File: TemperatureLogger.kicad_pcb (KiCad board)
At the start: 2 copper layers, 33 x 53 mm, 12 parts, among them J1 USB_A, SW1 RESET, SW2 A, SW3 B, SW4 MODE, U1 DHT11, U2 UA78M33_TO252, U3 ESP-12E, U4 TTL

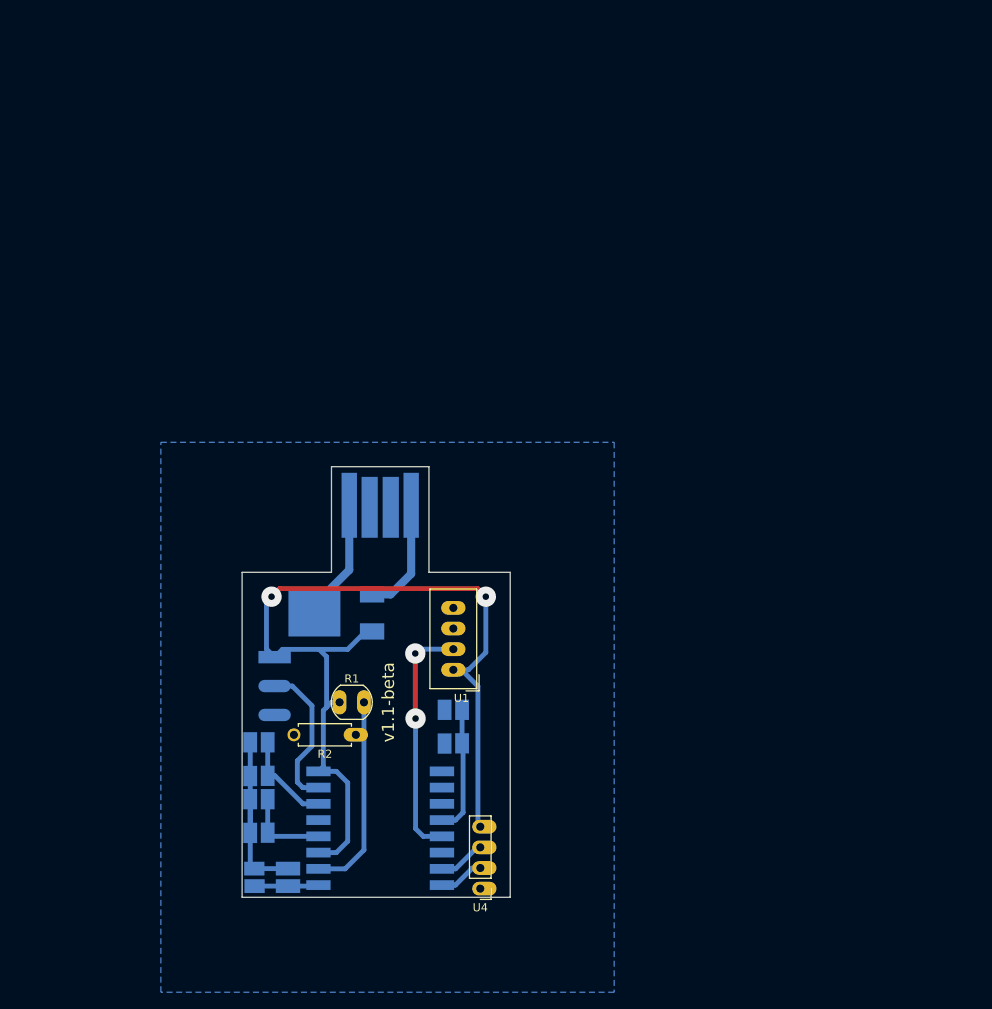
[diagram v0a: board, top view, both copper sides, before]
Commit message: Add main components
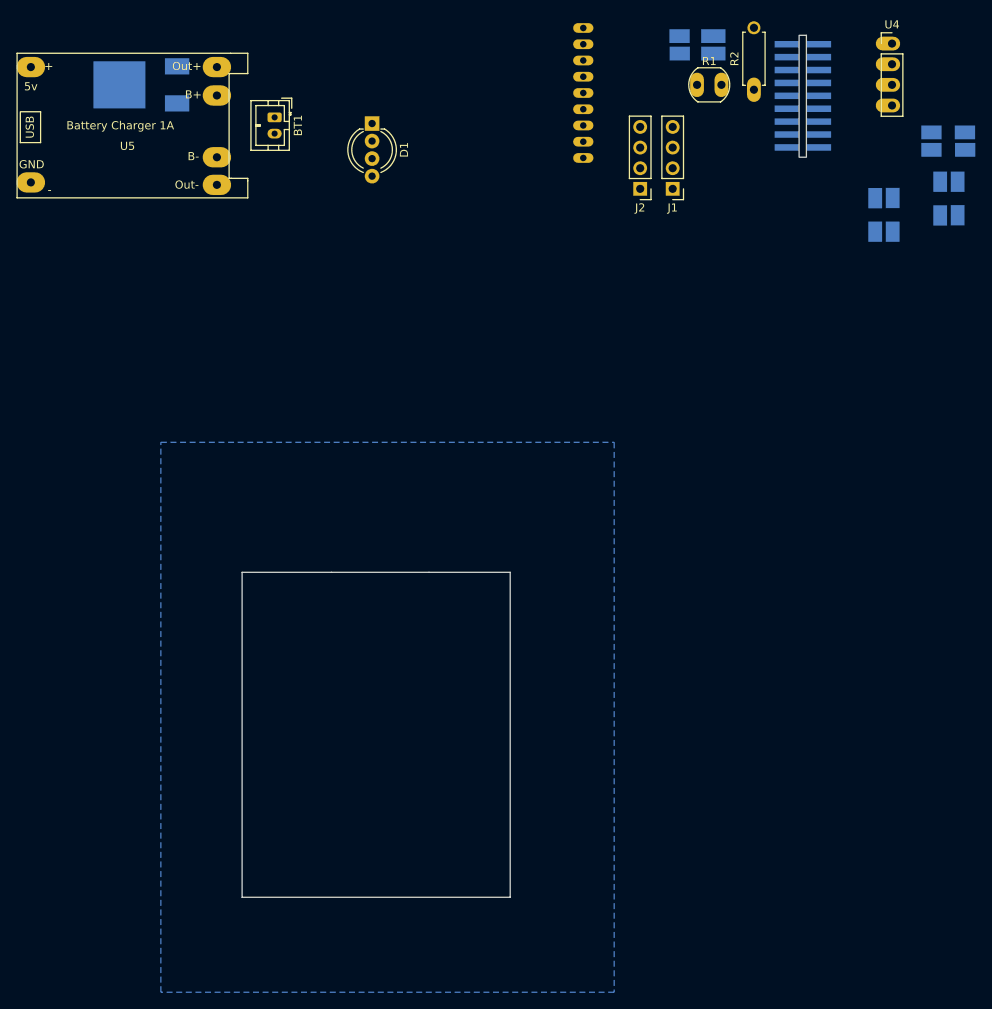
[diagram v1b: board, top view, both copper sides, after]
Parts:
- removed LIN1: LEDs_In, neopixel-strip:neopixel-strip
- removed U1: DHT11, Sensor:Aosong_DHT11_5.5x12.0_P2.54mm
- added BT1: Battery_Cell, Connector_JST:JST_PH_B2B-PH-K_1x02_P2.00mm_Vertical, F.Cu at (87.0, 25.0)
- added D1: WS2812B, LED_THT:LED_D5.0mm-4_RGB_Wide_Pins, F.Cu at (99.0, 25.8)
- added J2: I2C, Connector_PinHeader_2.54mm:PinHeader_1x04_P2.54mm_Vertical, F.Cu at (132.0, 33.8)
- added J3: Micro_SD_Card, sd-card:sd-card, B.Cu at (125.0, 22.0)
- added U5: tp4056, tp4056:tp4056, F.Cu at (68.0, 26.0)
- J1: value USB_A -> I2C; footprint usb-a-pcb:usb-a-pcb -> Connector_PinHeader_2.54mm:PinHeader_1x04_P2.54mm_Vertical; moved to F.Cu
- U3: value ESP-12E -> esp-01m; footprint RF_Module:ESP-12E -> esp-01m:esp-01m
- moved SW2 118.7 mm to (169.9, 27.9), turned to 0 degrees
- moved U4 115.7 mm to (163.0, 15.9), turned to 0 degrees
- moved SW1 115.1 mm to (138.9, 16.1)
- moved SW3 109.4 mm to (170.0, 35.0)
- moved U3 107.1 mm to (152.0, 22.4), turned to 180 degrees
- moved R2 93.3 mm to (146.0, 21.6), turned to 90 degrees
- moved R1 87.8 mm to (139.0, 21.0)
- moved SW4 82.3 mm to (162.0, 37.0), turned to 90 degrees
- moved U2 69.3 mm to (70.0, 21.0)
- moved J1 49.6 mm to (136.0, 33.8)
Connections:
- J1 pad 1: +5V -> +3V3
- J1 pad 2: unconnected-(J1-Pad2) -> GND
- J1 pad 3: unconnected-(J1-Pad3) -> I2C_CLK
- J1 pad 4: GND -> I2C_SDA
- R1 pad 2: Net-(U3-Pad2) -> Net-(R1-Pad2)
- R2 pad 1: Net-(U3-Pad2) -> Net-(R1-Pad2)
- U3 pad 1: Net-(SW1-Pad2) -> GND
- U3 pad 15: GND -> SPI_SS
- U3 pad 16: GND -> Net-(R1-Pad2)
- U3 pad 17: unconnected-(U3-Pad17) -> Net-(SW1-Pad2)
- U3 pad 18: Net-(SW4-Pad2) -> Net-(SW1-Pad2)
- U3 pad 2: Net-(U3-Pad2) -> +3V3
- U3 pad 3: +3V3 -> TX
- U3 pad 4: BUTTON-A -> RX
- U3 pad 5: unconnected-(U3-Pad5) -> NEOPIXEL
- U3 pad 6: BUTTON-B -> BUTTON-A
- U3 pad 7: NEOPIXEL -> BUTTON-B
- U3 pad 8: +3V3 -> Net-(SW4-Pad2)
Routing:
- net +3V3: track 114.1 -> 0.00 mm, vias 2 -> 0
- net GND: track 39.1 -> 0.00 mm
- net TEMP: track 30.1 -> 0.00 mm, vias 2 -> 0
- net Net-(U3-Pad2): track 25.7 -> 0.00 mm
- net NEOPIXEL: track 18.6 -> 0.00 mm
- net +5V: track 15.1 -> 0.00 mm
- net Net-(SW4-Pad2): track 14.9 -> 0.00 mm
- net BUTTON-B: track 11.8 -> 0.00 mm
- net BUTTON-A: track 10.6 -> 0.00 mm
- net Net-(SW1-Pad2): track 7.92 -> 0.00 mm
- net RX: track 5.81 -> 0.00 mm
- net TX: track 5.59 -> 0.00 mm
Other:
- board size 33 x 53 mm -> 33 x 40 mm
- board text removed: "COVER!"
- board text removed: "TODO: - Neopixel needs more space and flat underground - Switches pads need to move to the outside of the switch - Fix DHT11 - Neopixel add header 3 x connector"
- board text removed: "v1.1-beta"

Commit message: Add bme280 sensor and as12ap switch
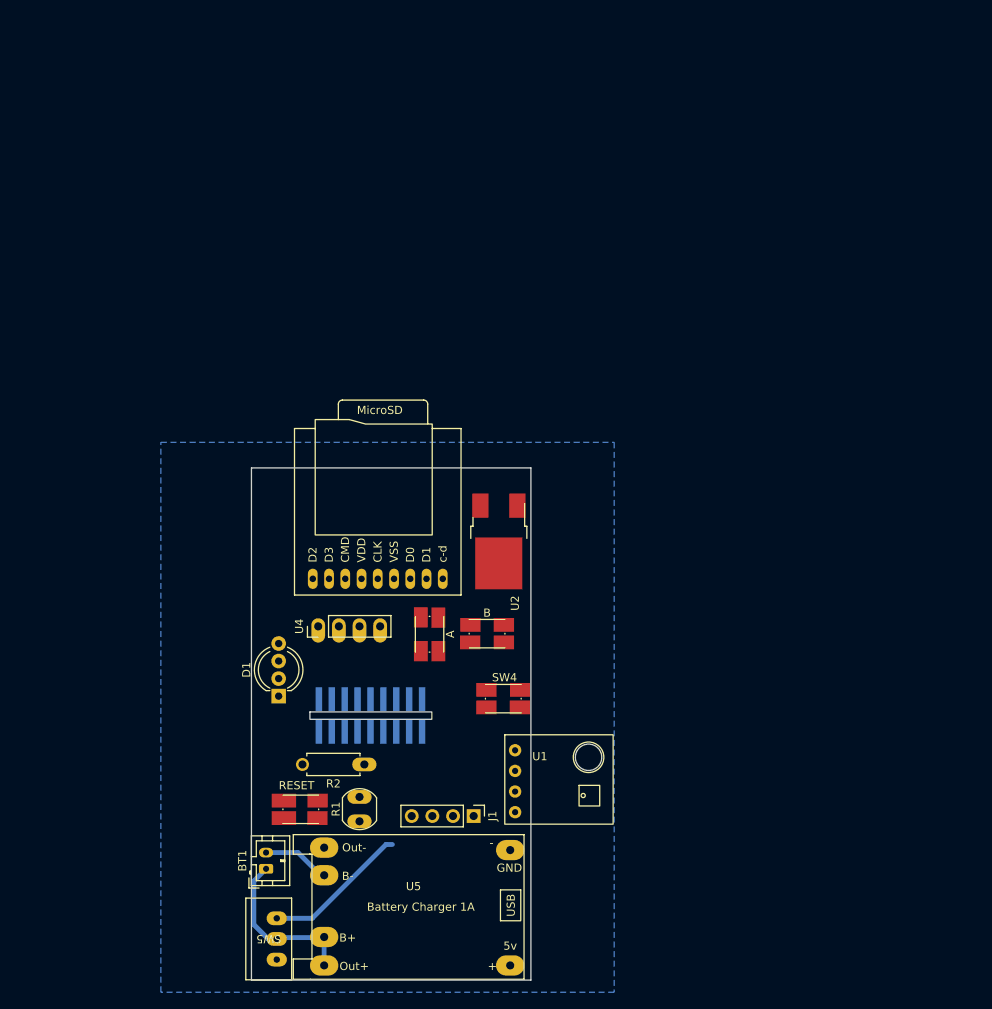
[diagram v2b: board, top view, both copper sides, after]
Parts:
- removed J2: I2C, Connector_PinHeader_2.54mm:PinHeader_1x04_P2.54mm_Vertical
- added SW5: POWER, as12ap:as12ap, F.Cu at (87.3, 128.7)
- added U1: bme280, bme280:bme280, F.Cu at (116.6, 106.7)
- J3, SW1, SW2, SW3, SW4, U2: moved to F.Cu
- moved SW1 106.0 mm to (90.2, 110.2), turned to 0 degrees
- moved U5 103.1 mm to (105.0, 122.2), turned to 180 degrees
- moved U4 100.7 mm to (92.4, 87.7), turned to 90 degrees
- moved R1 99.7 mm to (97.5, 111.7), turned to 90 degrees
- moved R2 95.9 mm to (98.0, 104.7), turned to 180 degrees
- moved U3 93.0 mm to (98.8, 98.7), turned to -90 degrees
- moved BT1 92.5 mm to (86.0, 117.5), turned to 90 degrees
- moved SW2 88.1 mm to (106.1, 88.6), turned to 90 degrees
- moved J1 81.0 mm to (111.5, 111.0), turned to -90 degrees
- moved SW3 78.1 mm to (113.2, 88.5), turned to 180 degrees
- moved SW4 75.8 mm to (115.2, 96.5), turned to 0 degrees
- moved U2 72.2 mm to (114.6, 77.8), turned to -90 degrees
- moved D1 71.4 mm to (87.5, 96.2), turned to 90 degrees
- moved J3 64.9 mm to (99.7, 81.8), turned to 90 degrees
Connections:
- U2 pad 3: +3V3 -> unconnected-(U2-Pad3)
- U5 pad 3: +5V -> Net-(BT1-Pad1)
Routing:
- net Net-(BT1-Pad1): track 0.00 -> 20.2 mm
- net +5V: track 0.00 -> 18.0 mm
- net Net-(BT1-Pad2): track 0.00 -> 8.31 mm
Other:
- board size 33 x 40 mm -> 34.4 x 63 mm

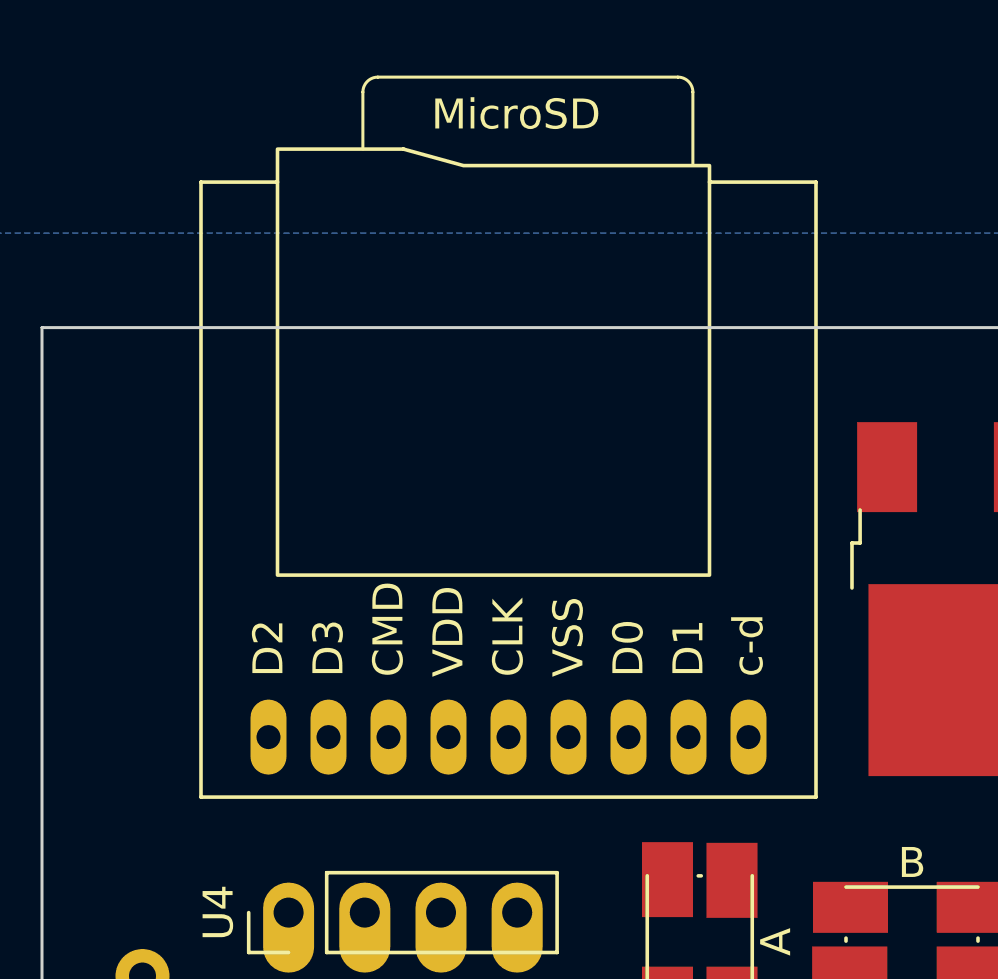
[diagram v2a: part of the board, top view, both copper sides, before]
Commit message: Update sd card module
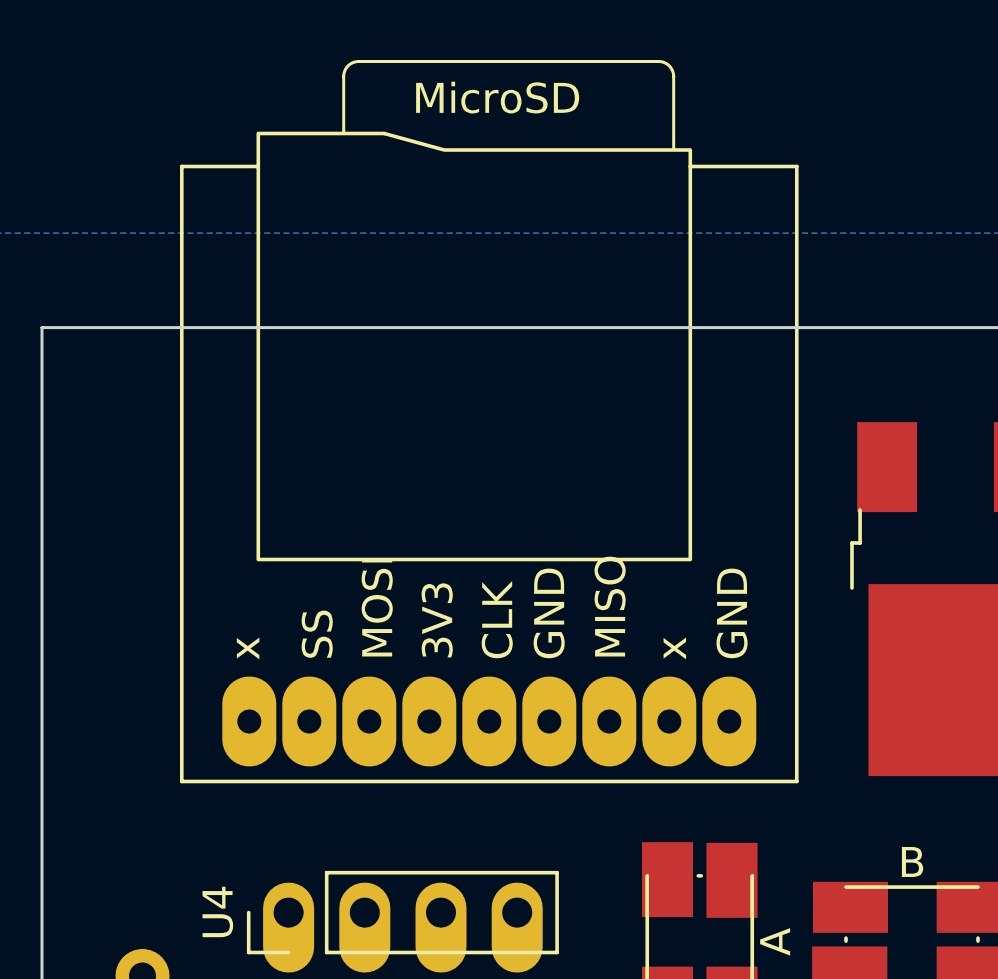
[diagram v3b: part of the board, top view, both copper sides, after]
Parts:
- moved J3 0.82 mm to (99.1, 81.3)

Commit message: First routing
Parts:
- removed R1: R_Photo, OptoDevice:R_LDR_5.0x4.1mm_P3mm_Vertical
- removed R2: 10k, Resistor_THT:R_Axial_DIN0207_L6.3mm_D2.5mm_P7.62mm_Horizontal
- removed SW2: A, Button_Switch_SMD:SW_Push_1P1T_NO_Vertical_Wuerth_434133025816
- removed SW3: B, Button_Switch_SMD:SW_Push_1P1T_NO_Vertical_Wuerth_434133025816
- SW1, SW4, U2: moved to B.Cu
- moved U2 49.5 mm to (100.6, 125.3)
- moved U1 31.6 mm to (86.4, 97.6), turned to 180 degrees
- moved U4 28.7 mm to (108.0, 111.8), turned to -90 degrees
- moved SW1 26.6 mm to (111.4, 94.1), turned to 90 degrees
- moved J1 23.3 mm to (90.2, 101.4), turned to 180 degrees
- moved D1 14.2 mm to (93.2, 109.2), turned to 180 degrees
- moved SW4 10.2 mm to (114.3, 106.7), turned to 90 degrees
- moved U3 1.86 mm to (100.6, 98.8), turned to 90 degrees
- moved J3 1.59 mm to (100.6, 81.3)
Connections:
- U2 pad 3: unconnected-(U2-Pad3) -> +3V3
- U5 pad 1: VBUS -> unconnected-(U5-Pad1)
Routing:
- net +3V3: track 0.00 -> 89.8 mm, vias 0 -> 4
- net Net-(U3-Pad8): track 0.00 -> 26.2 mm, vias 0 -> 2
- net SPI_MISO: track 0.00 -> 22.7 mm, vias 0 -> 2
- net SPI_SS: track 0.00 -> 22.5 mm, vias 0 -> 2
- net NEOPIXEL: track 0.00 -> 20.3 mm, vias 0 -> 2
- net SPI_MOSI: track 0.00 -> 16.6 mm
- net SPI_CLK: track 0.00 -> 15.6 mm
- net I2C_SDA: track 0.00 -> 12.3 mm
- net TX: track 0.00 -> 11.7 mm
- net RX: track 0.00 -> 11.2 mm
- net Net-(U3-Pad17): track 0.00 -> 9.33 mm
- net I2C_CLK: track 0.00 -> 8.18 mm
- net +5V: track 18.0 -> 26.1 mm
- net GND: track 0.00 -> 7.41 mm
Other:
- board size 34.4 x 63 mm -> 34.4 x 54.2 mm

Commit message: Addes todos
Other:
- board text added: "TODO: Maybe rotate the bme and make a regular jst plug"
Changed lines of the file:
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@@
     (effects (font (size 1.5 1.5) (thickness 0.3)) (justify left))
+  )
+  (gr_text "TODO: Maybe rotate the bme and make a regular jst plug" (at 102.05 48.55) (layer "F.Fab")
+    (effects (font (size 1.5 1.5) (thickness 0.3)))
   )
   (segment (start 88.9 110.69) (end 88.9 109.22) (width 0.4) (layer "B.Cu") (net 1))
